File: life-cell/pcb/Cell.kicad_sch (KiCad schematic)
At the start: 7 parts, among them J5 UPDI, SW1 Toggle, U1 ATtiny404-SS

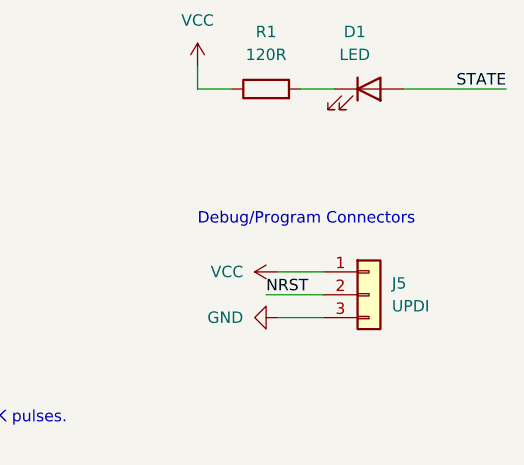
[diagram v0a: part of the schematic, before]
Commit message: Switch to "symmetric" connector layout.
Each side has half male pins and half female pins, for a truly
symmetric experience!
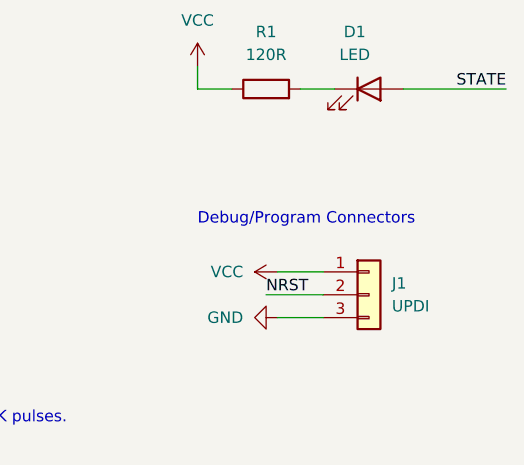
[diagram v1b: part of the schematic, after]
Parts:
- renumbered J5 to J1
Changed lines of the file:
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@@
   (symbol (lib_id "Connector_Generic:Conn_01x03") (at 191.77 100.33 0) (unit 1)
     (in_bom yes) (on_board yes) (fields_autoplaced)
-    (property "Reference" "J5" (id 0) (at 194.31 99.0599 0)
+    (property "Reference" "J1" (id 0) (at 194.31 99.0599 0)
       (effects (font (size 1.27 1.27)) (justify left))
     )
